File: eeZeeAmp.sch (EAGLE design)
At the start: 19 parts, among them IC1 LM386

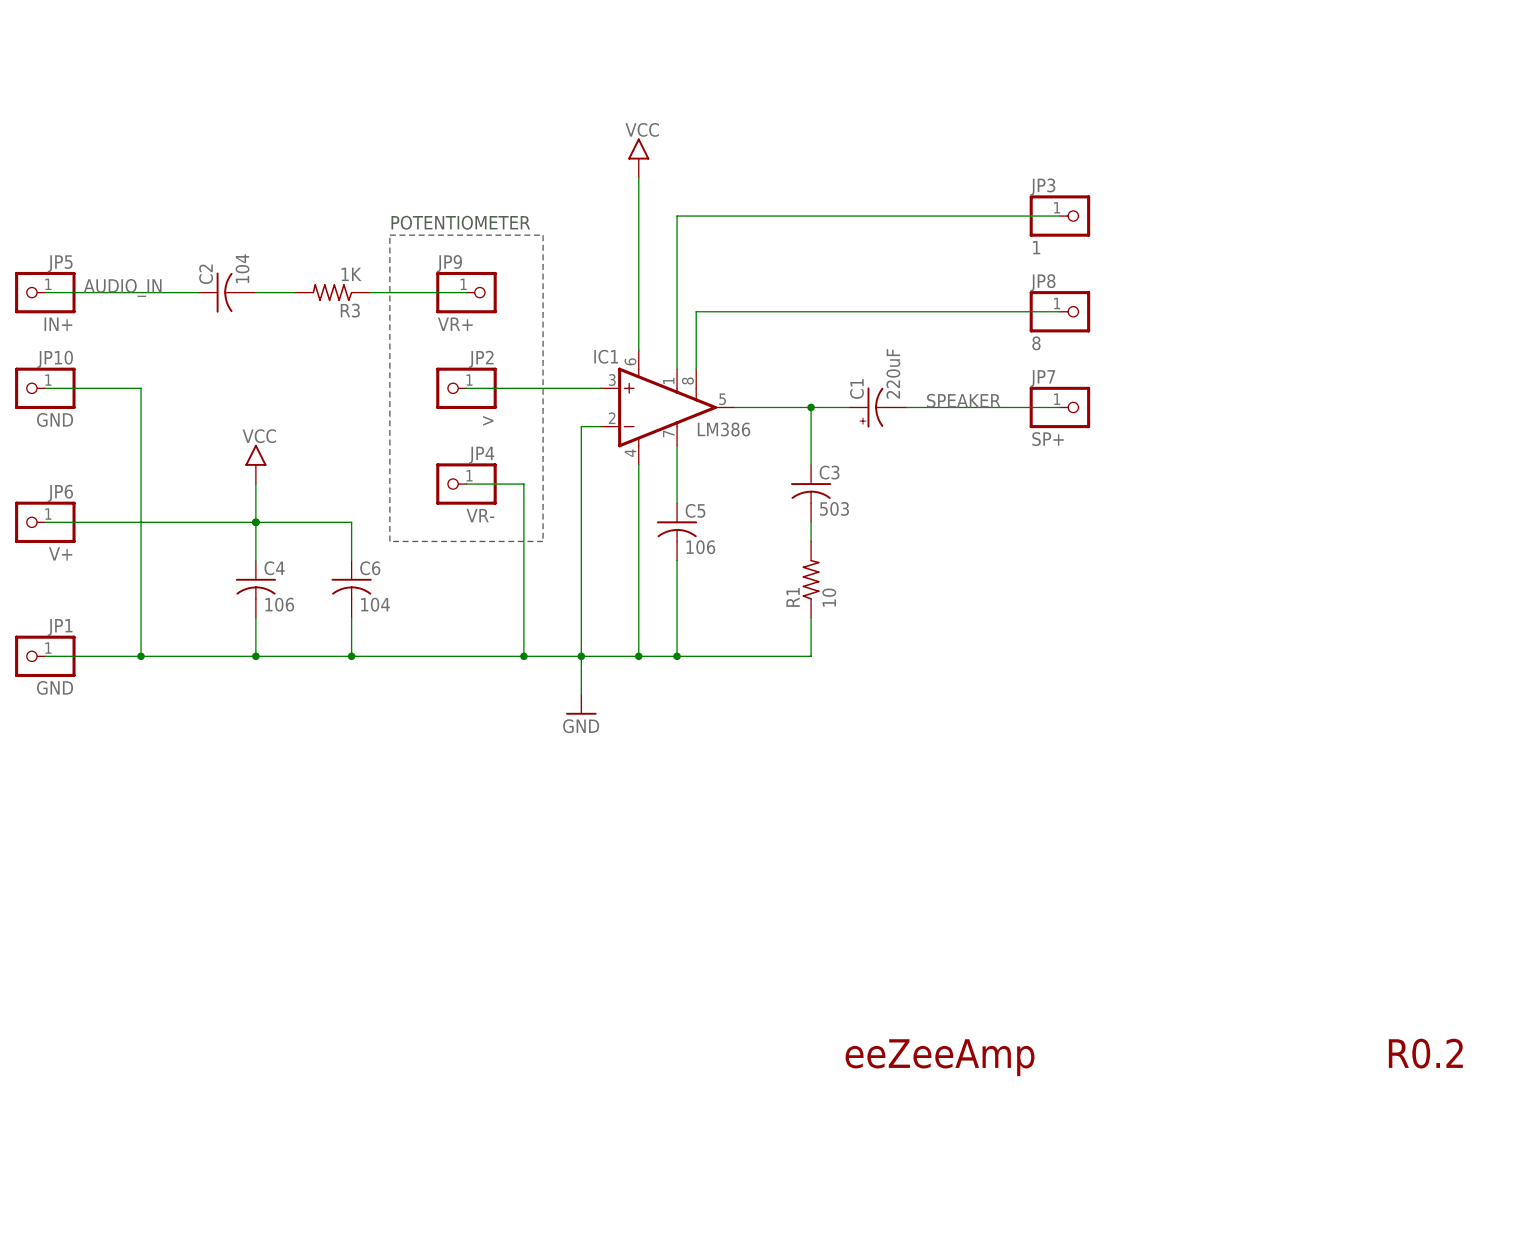
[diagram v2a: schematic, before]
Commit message: Added title, OSHW logo on both sheets, relabeled gnd, audio in gnd pin header, added gain label, added cc
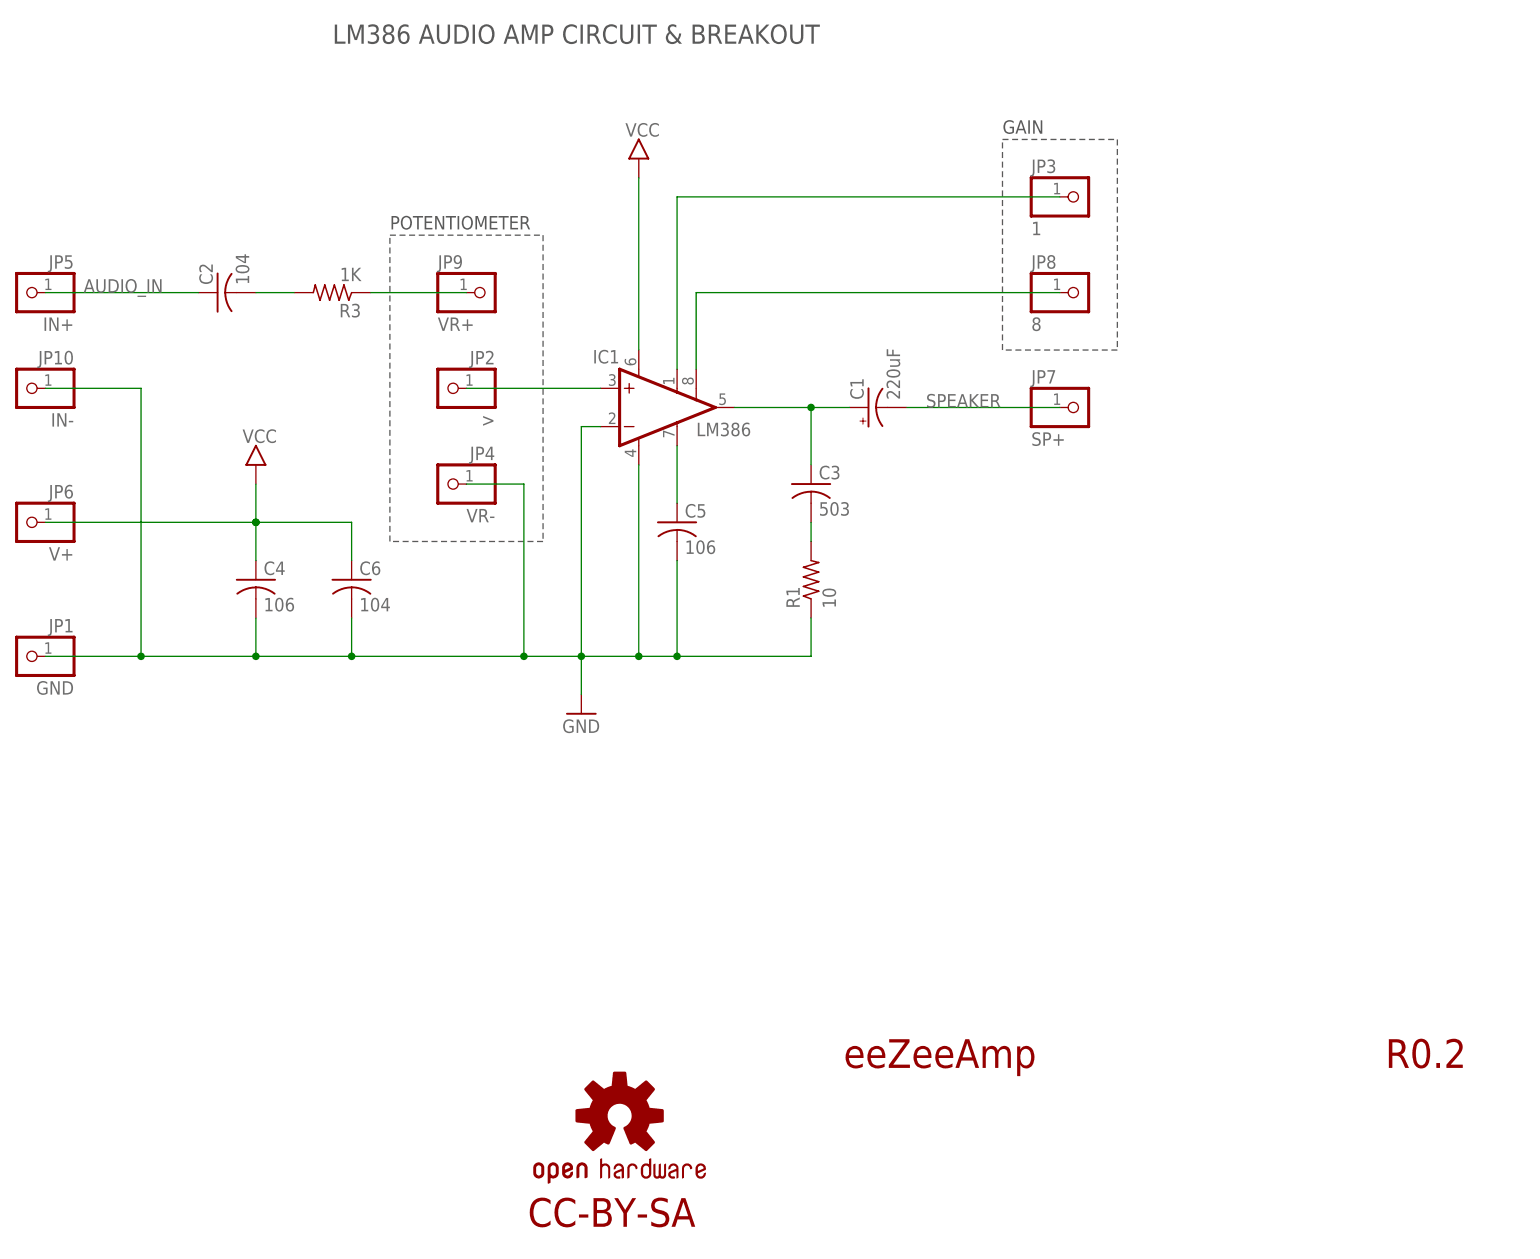
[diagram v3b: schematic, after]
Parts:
- added LOGO2: OSHW-LOGOS, SparkFun-Aesthetics:OSHW-LOGOS
- JP10: value GND -> IN-
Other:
- note added: "CC-BY-SA"
- note added: "GAIN"
- note added: "LM386 AUDIO AMP CIRCUIT & BREAKOUT"
- moved on the sheet: JP3, JP8
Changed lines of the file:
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@@
 <layer number="54" name="bPadExt" color="1" fill="1" visible="no" active="no"/>
 <layer number="56" name="wert" color="7" fill="1" visible="no" active="no"/>
+<layer number="57" name="tCAD" color="7" fill="1" visible="no" active="no"/>
+<layer number="59" name="tCarbon" color="7" fill="1" visible="no" active="no"/>
+<layer number="60" name="bCarbon" color="7" fill="1" visible="no" active="no"/>
 <layer number="90" name="Modules" color="5" fill="1" visible="yes" active="yes"/>
 <layer number="91" name="Nets" color="2" fill="1" visible="yes" active="yes"/>
@@
 <layer number="106" name="bPlate" color="7" fill="1" visible="no" active="yes"/>
 <layer number="107" name="Crop" color="7" fill="1" visible="no" active="yes"/>
+<layer number="108" name="tplace-old" color="10" fill="1" visible="yes" active="yes"/>
+<layer number="109" name="ref-old" color="11" fill="1" visible="yes" active="yes"/>
+<layer number="110" name="fp0" color="7" fill="1" visible="yes" active="yes"/>
+<layer number="111" name="LPC17xx" color="7" fill="1" visible="yes" active="yes"/>
+<layer number="112" name="tSilk" color="7" fill="1" visible="yes" active="yes"/>
+<layer number="113" name="IDFDebug" color="4" fill="1" visible="yes" active="yes"/>
 <layer number="116" name="Patch_BOT" color="9" fill="4" visible="no" active="yes"/>
 <layer number="121" name="_tsilk" color="7" fill="1" visible="no" active="yes"/>
 <layer number="122" name="_bsilk" color="7" fill="1" visible="no" active="yes"/>
+<layer number="123" name="tTestmark" color="7" fill="1" visible="yes" active="yes"/>
+<layer number="124" name="bTestmark" color="7" fill="1" visible="yes" active="yes"/>
 <layer number="125" name="_tNames" color="7" fill="1" visible="no" active="yes"/>
+<layer number="126" name="_bNames" color="7" fill="1" visible="yes" active="yes"/>
+<layer number="127" name="_tValues" color="7" fill="1" visible="yes" active="yes"/>
+<layer number="128" name="_bValues" color="7" fill="1" visible="yes" active="yes"/>
+<layer number="129" name="Mask" color="7" fill="1" visible="yes" active="yes"/>
+<layer number="131" name="tAdjust" color="7" fill="1" visible="yes" active="yes"/>
+<layer number="132" name="bAdjust" color="7" fill="1" visible="yes" active="yes"/>
 <layer number="144" name="Drill_legend" color="7" fill="1" visible="no" active="yes"/>
+<layer number="150" name="Notes" color="7" fill="1" visible="yes" active="yes"/>
 <layer number="151" name="HeatSink" color="7" fill="1" visible="no" active="yes"/>
+<layer number="152" name="_bDocu" color="7" fill="1" visible="yes" active="yes"/>
+<layer number="153" name="FabDoc1" color="7" fill="1" visible="yes" active="yes"/>
+<layer number="154" name="FabDoc2" color="7" fill="1" visible="yes" active="yes"/>
+<layer number="155" name="FabDoc3" color="7" fill="1" visible="yes" active="yes"/>
+<layer number="199" name="Contour" color="7" fill="1" visible="yes" active="yes"/>
 <layer number="200" name="200bmp" color="1" fill="10" visible="no" active="yes"/>
 <layer number="201" name="201bmp" color="2" fill="10" visible="no" active="yes"/>
@@
 <layer number="223" name="223bmp" color="24" fill="1" visible="no" active="no"/>
 <layer number="224" name="224bmp" color="25" fill="1" visible="no" active="no"/>
+<layer number="225" name="225bmp" color="7" fill="1" visible="yes" active="yes"/>
+<layer number="226" name="226bmp" color="7" fill="1" visible="yes" active="yes"/>
+<layer number="227" name="227bmp" color="7" fill="1" visible="yes" active="yes"/>
+<layer number="228" name="228bmp" color="7" fill="1" visible="yes" active="yes"/>
+<layer number="229" name="229bmp" color="7" fill="1" visible="yes" active="yes"/>
+<layer number="230" name="230bmp" color="7" fill="1" visible="yes" active="yes"/>
 <layer number="231" name="Eagle3D_PG1" color="14" fill="1" visible="no" active="yes"/>
 <layer number="232" name="Eagle3D_PG2" color="14" fill="2" visible="no" active="yes"/>
 <layer number="233" name="Eagle3D_PG3" color="14" fill="4" visible="no" active="yes"/>
+<layer number="248" name="Housing" color="7" fill="1" visible="yes" active="yes"/>
+<layer number="249" name="Edge" color="7" fill="1" visible="yes" active="yes"/>
 <layer number="250" name="Descript" color="7" fill="1" visible="no" active="yes"/>
 <layer number="251" name="SMDround" color="7" fill="1" visible="no" active="yes"/>
 <layer number="254" name="OrgLBR" color="7" fill="1" visible="no" active="yes"/>
+<layer number="255" name="routoute" color="7" fill="1" visible="yes" active="yes"/>
 </layers>
 <schematic xreflabel="%F%N/%S.%C%R" xrefpart="/%S.%C%R">
@@
 <part name="JP2" library="pinhead-2" deviceset="PINHD-1X01" device="_2.54-S" value="&gt;"/>
 <part name="JP9" library="pinhead-2" deviceset="PINHD-1X01" device="_2.54-S" value="VR+"/>
-<part name="JP10" library="pinhead-2" deviceset="PINHD-1X01" device="_2.54-S" value="GND"/>
+<part name="JP10" library="pinhead-2" deviceset="PINHD-1X01" device="_2.54-S" value="IN-"/>
+<part name="LOGO2" library="SparkFun-Aesthetics" deviceset="OSHW-LOGO" device="S"/>
 </parts>
 <sheets>
@@
 <wire x1="99.06" y1="93.98" x2="99.06" y2="134.62" width="0.1524" layer="97" style="shortdash"/>
 <text x="99.06" y="135.382" size="1.778" layer="97">POTENTIOMETER</text>
+<text x="91.44" y="160.02" size="2.54" layer="97">LM386 AUDIO AMP CIRCUIT &amp; BREAKOUT</text>
+<wire x1="180.34" y1="147.32" x2="195.58" y2="147.32" width="0.1524" layer="97" style="shortdash"/>
+<wire x1="195.58" y1="147.32" x2="195.58" y2="119.38" width="0.1524" layer="97" style="shortdash"/>
+<wire x1="195.58" y1="119.38" x2="180.34" y2="119.38" width="0.1524" layer="97" style="shortdash"/>
+<wire x1="180.34" y1="119.38" x2="180.34" y2="147.32" width="0.1524" layer="97" style="shortdash"/>
+<text x="180.34" y="148.082" size="1.778" layer="97">GAIN</text>
+<text x="117.348" y="3.048" size="3.81" layer="94" ratio="20">CC-BY-SA</text>
 </plain>
 <instances>
@@
 <instance part="JP7" gate="A" x="190.5" y="111.76"/>
 <instance part="JP1" gate="A" x="50.8" y="78.74" rot="MR0"/>
-<instance part="JP3" gate="A" x="190.5" y="137.16"/>
-<instance part="JP8" gate="A" x="190.5" y="124.46"/>
+<instance part="JP3" gate="A" x="190.5" y="139.7"/>
+<instance part="JP8" gate="A" x="190.5" y="127"/>
 <instance part="JP4" gate="A" x="106.68" y="101.6" rot="MR0"/>
 <instance part="JP2" gate="A" x="106.68" y="114.3" rot="MR0"/>
 <instance part="JP9" gate="A" x="111.76" y="127"/>
 <instance part="JP10" gate="A" x="50.8" y="114.3" rot="MR0"/>
+<instance part="LOGO2" gate="G$1" x="129.54" y="17.78"/>
 </instances>
 <busses>
@@
 <segment>
 <pinref part="IC1" gate="G$1" pin="GAIN@1"/>
-<wire x1="137.16" y1="116.84" x2="137.16" y2="137.16" width="0.1524" layer="91"/>
-<wire x1="137.16" y1="137.16" x2="187.96" y2="137.16" width="0.1524" layer="91"/>
+<wire x1="137.16" y1="116.84" x2="137.16" y2="139.7" width="0.1524" layer="91"/>
+<wire x1="137.16" y1="139.7" x2="187.96" y2="139.7" width="0.1524" layer="91"/>
 <pinref part="JP3" gate="A" pin="1"/>
 </segment>
@@
 <segment>
 <pinref part="IC1" gate="G$1" pin="GAIN@2"/>
-<wire x1="139.7" y1="116.84" x2="139.7" y2="124.46" width="0.1524" layer="91"/>
-<wire x1="139.7" y1="124.46" x2="187.96" y2="124.46" width="0.1524" layer="91"/>
+<wire x1="139.7" y1="116.84" x2="139.7" y2="127" width="0.1524" layer="91"/>
+<wire x1="139.7" y1="127" x2="187.96" y2="127" width="0.1524" layer="91"/>
 <pinref part="JP8" gate="A" pin="1"/>
 </segment>

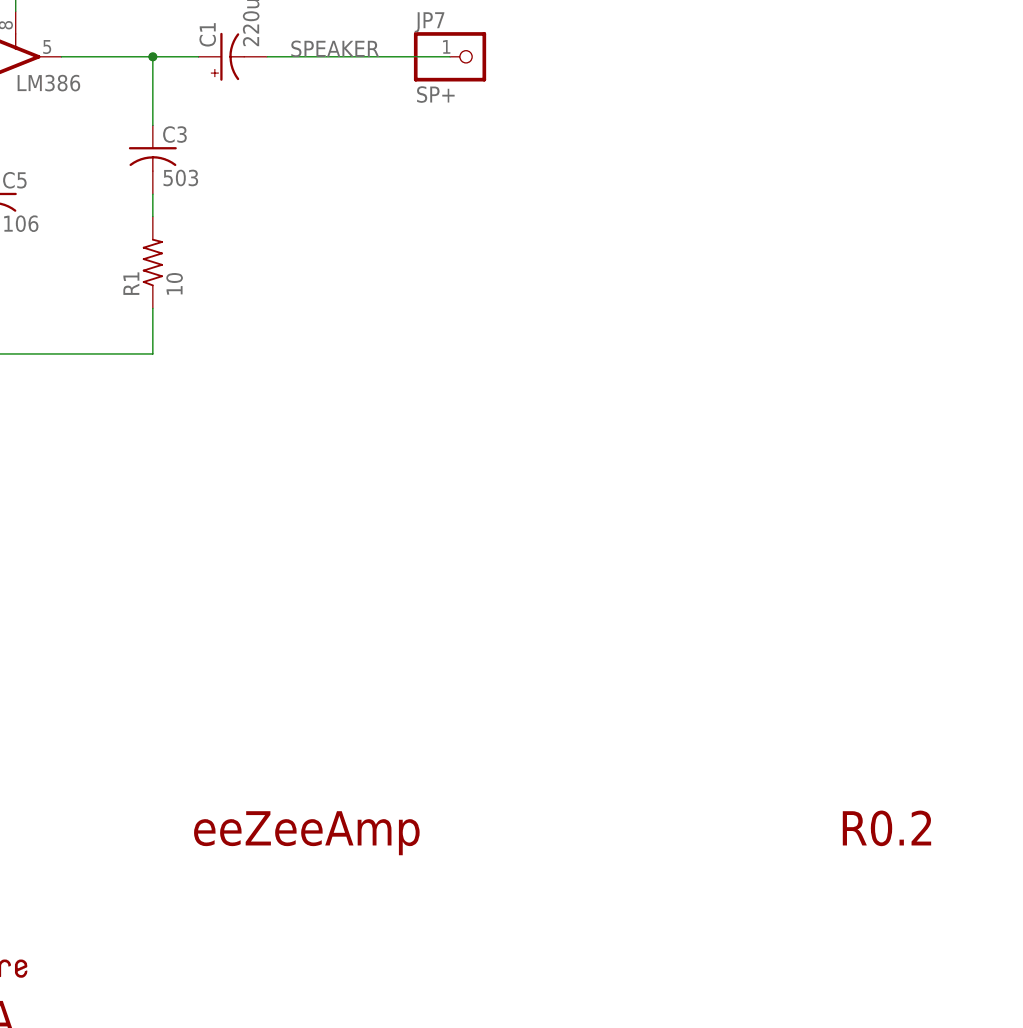
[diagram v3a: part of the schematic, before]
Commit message: Changed 503 cap to more common value 473
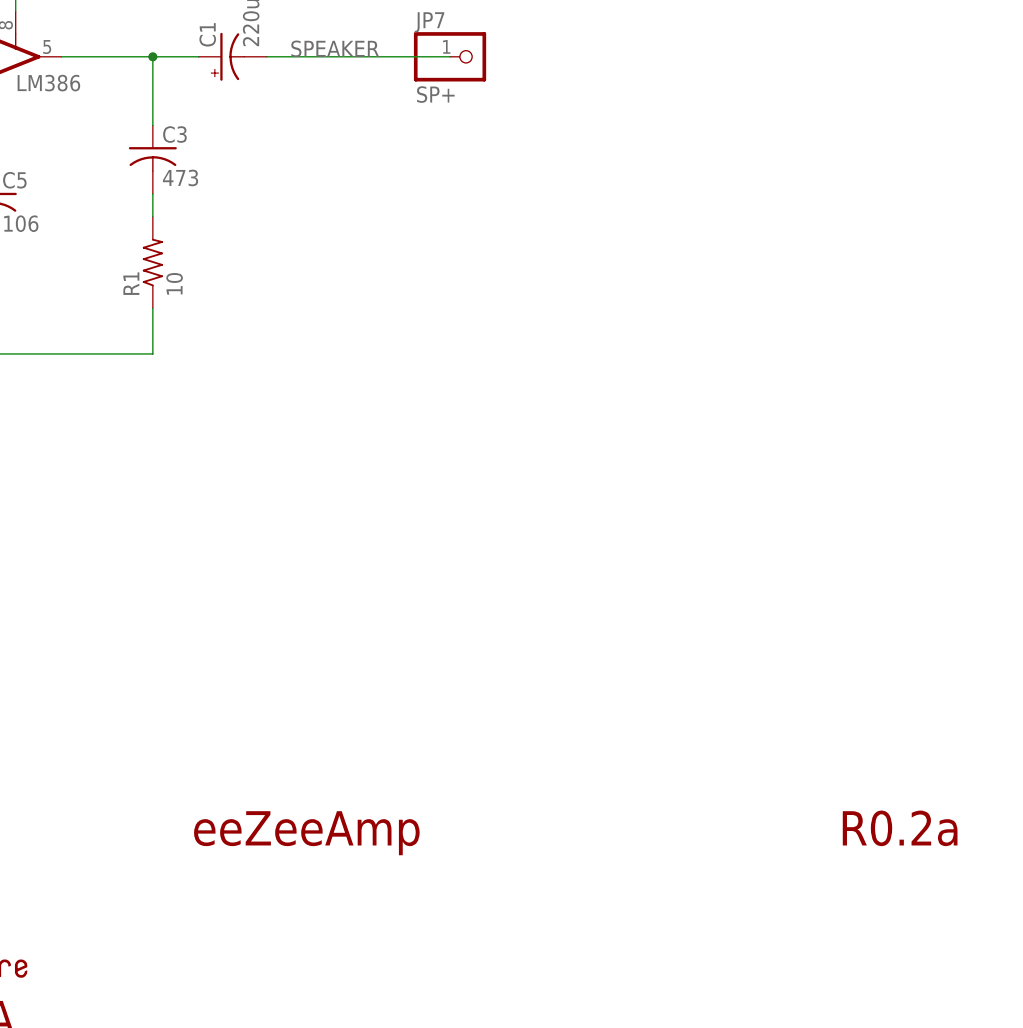
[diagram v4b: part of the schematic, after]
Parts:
- C3: value 503 -> 473
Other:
- note added: "R0.2a"
- note removed: "R0.2"
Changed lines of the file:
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@@
 <part name="C1" library="rcl" deviceset="CPOL-US" device="E3.5-8" value="220uF"/>
 <part name="C2" library="rcl" deviceset="C-US" device="C0603" value="104"/>
-<part name="C3" library="rcl" deviceset="C-US" device="C0603" value="503"/>
+<part name="C3" library="rcl" deviceset="C-US" device="C0603" value="473"/>
 <part name="R1" library="resistor" deviceset="R-US_" device="R0603" value="10"/>
 <part name="R3" library="resistor" deviceset="R-US_" device="R0603" value="1K"/>
@@
 <plain>
 <text x="159.258" y="24.13" size="3.81" layer="94">eeZeeAmp</text>
-<text x="231.14" y="24.13" size="3.81" layer="94">R0.2</text>
+<text x="231.14" y="24.13" size="3.81" layer="94">R0.2a</text>
 <wire x1="99.06" y1="134.62" x2="119.38" y2="134.62" width="0.1524" layer="97" style="shortdash"/>
 <wire x1="119.38" y1="134.62" x2="119.38" y2="93.98" width="0.1524" layer="97" style="shortdash"/>
